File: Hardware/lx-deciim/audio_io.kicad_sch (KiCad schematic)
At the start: 35 parts, among them J13 AudioJack2_SwitchT, J14 AudioJack2_SwitchT, J15 AudioJack2_SwitchT, J16 AudioJack2_SwitchT, U5 TL074, U6 MCP6004

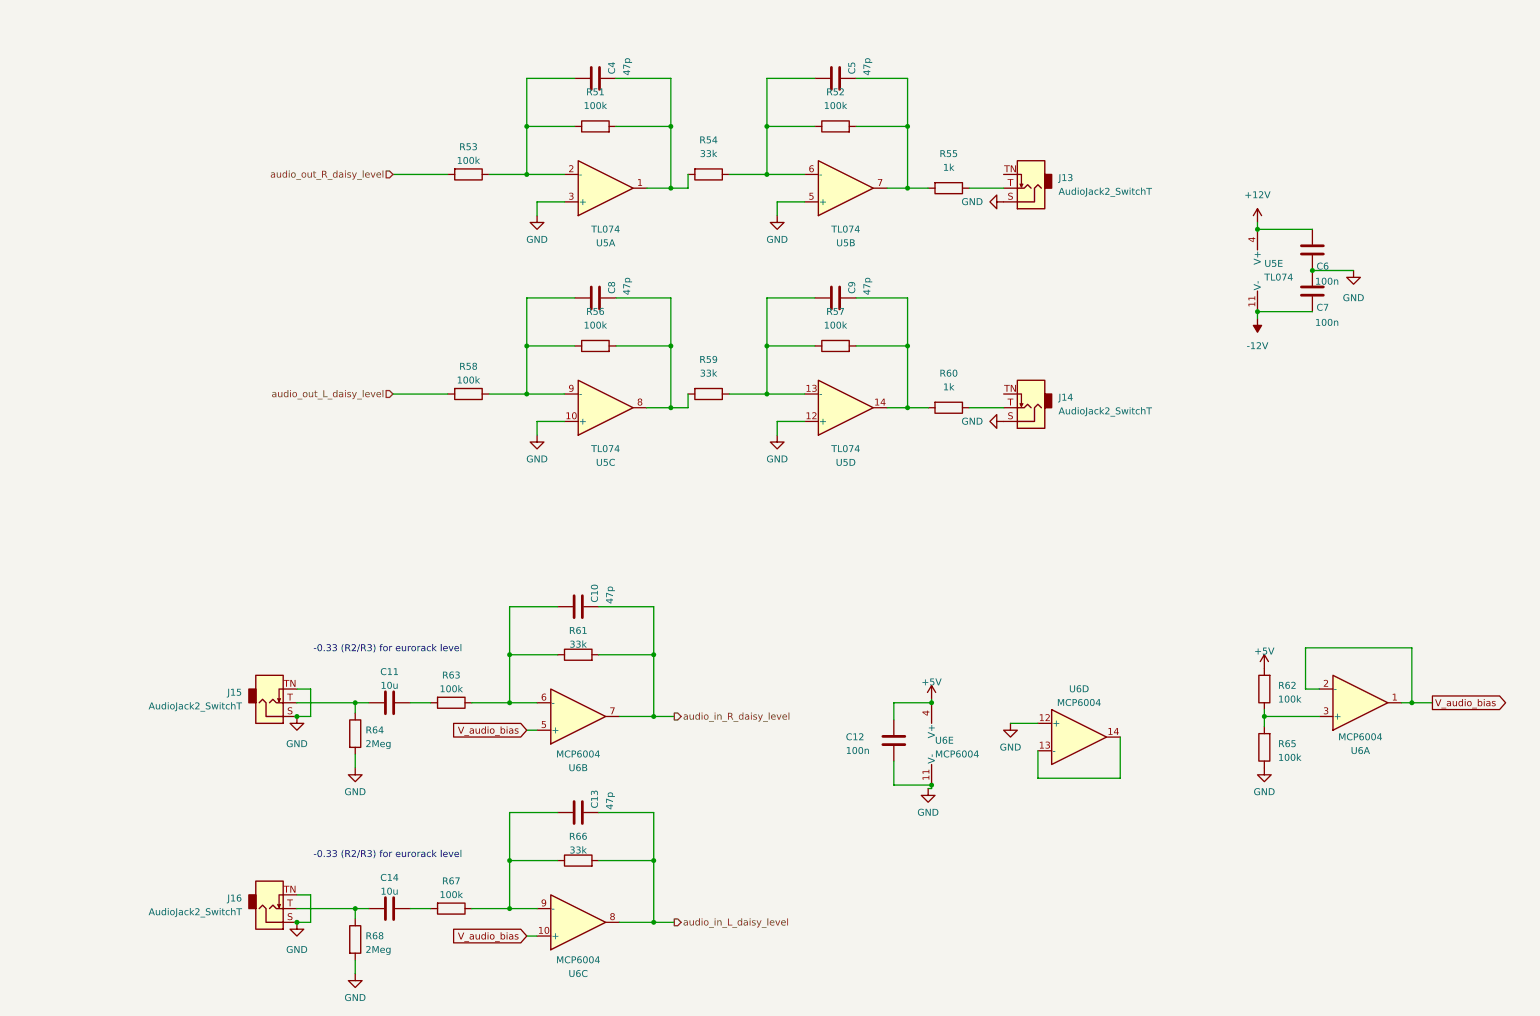
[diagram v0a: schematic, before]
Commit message: feature: first draft routing
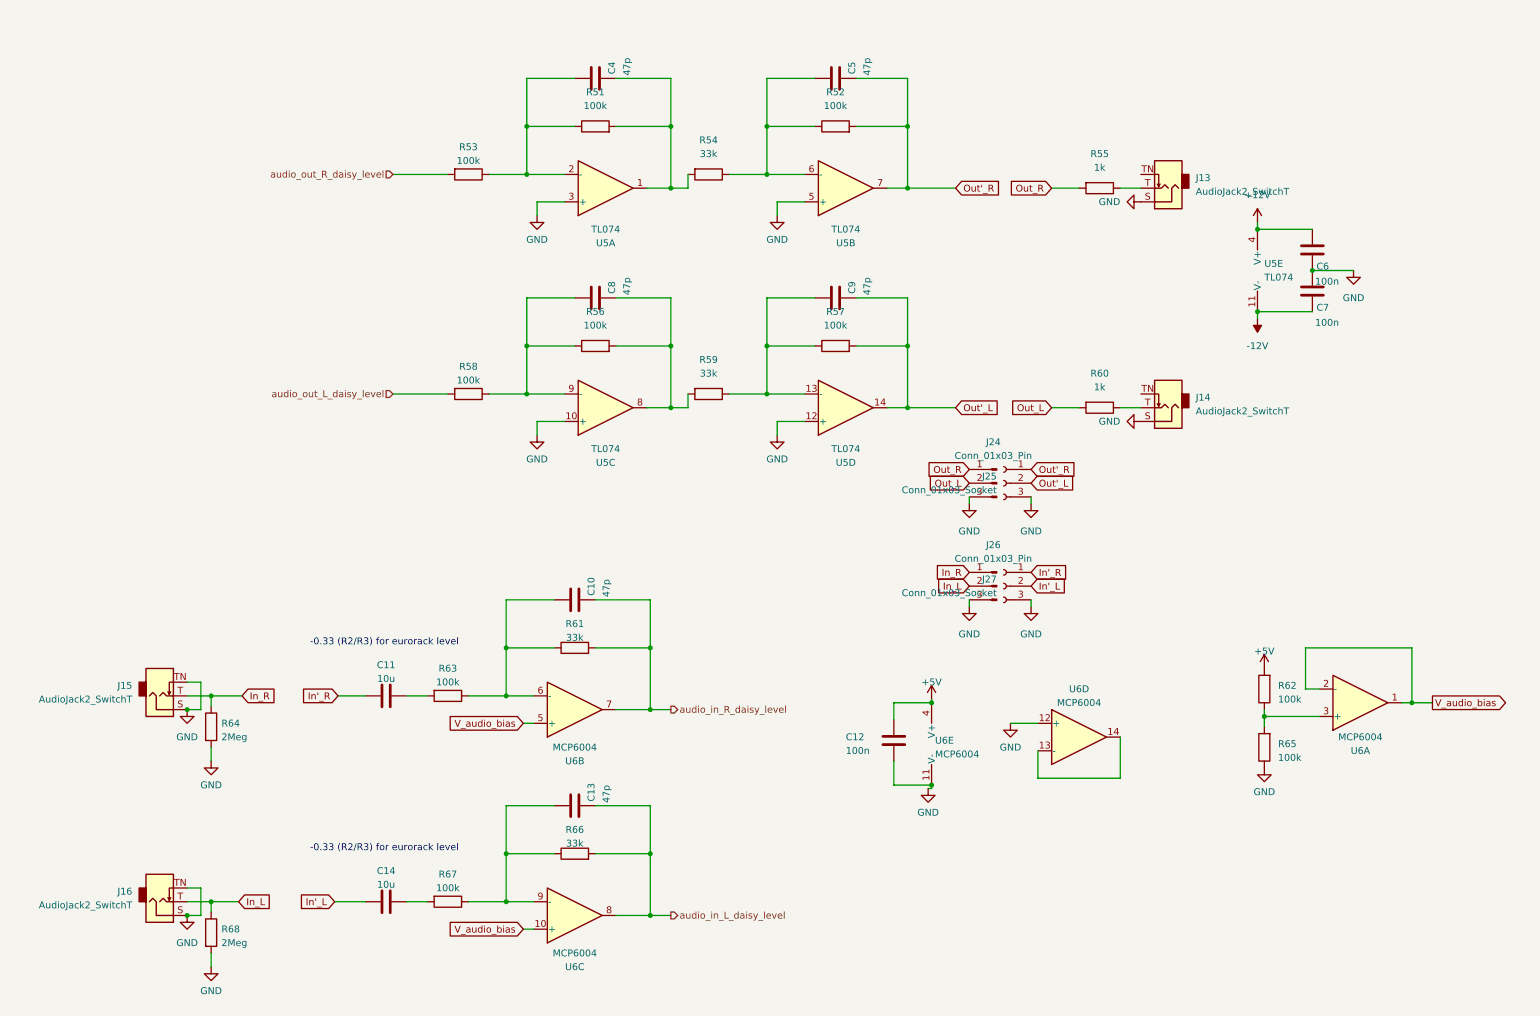
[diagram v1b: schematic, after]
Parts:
- added J24, J26: Conn_01x03_Pin, Connector_PinHeader_2.54mm:PinHeader_1x03_P2.54mm_Vertical, symbol Connector:Conn_01x03_Pin
- added J25, J27: Conn_01x03_Socket, Connector_PinSocket_2.54mm:PinSocket_1x03_P2.54mm_Vertical, symbol Connector:Conn_01x03_Socket
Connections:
- net GND: now also J24.3 (Pin_3), J25.3 (Pin_3), J26.3 (Pin_3), J27.3 (Pin_3)
- net Out'_R: now reaches C5.2, R52.2, U5.7
- net Out'_R: now also J25.1 (Pin_1); no longer R55.2
- net Out'_L: now reaches C9.2, R57.2, U5.14
- net Out'_L: now also J25.2 (Pin_2); no longer R60.2
- net In_L: now reaches J16.T, R68.1
- net In_L: now also J26.2 (Pin_2); no longer C14.1
- net In_R: now reaches J15.T, R64.1
- net In_R: now also J26.1 (Pin_1); no longer C11.1
- new net In'_L: C14.1, J27.2 (Pin_2)
- new net In'_R: C11.1, J27.1 (Pin_1)
- new net Out_L: J24.2 (Pin_2), R60.2
- new net Out_R: J24.1 (Pin_1), R55.2
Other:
- moved on the sheet: C10, C11, C13, C14, J13, J14, J15, J16, R55, R60, R61, R63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

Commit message: feature: prep files for export (fill bom, gerber)
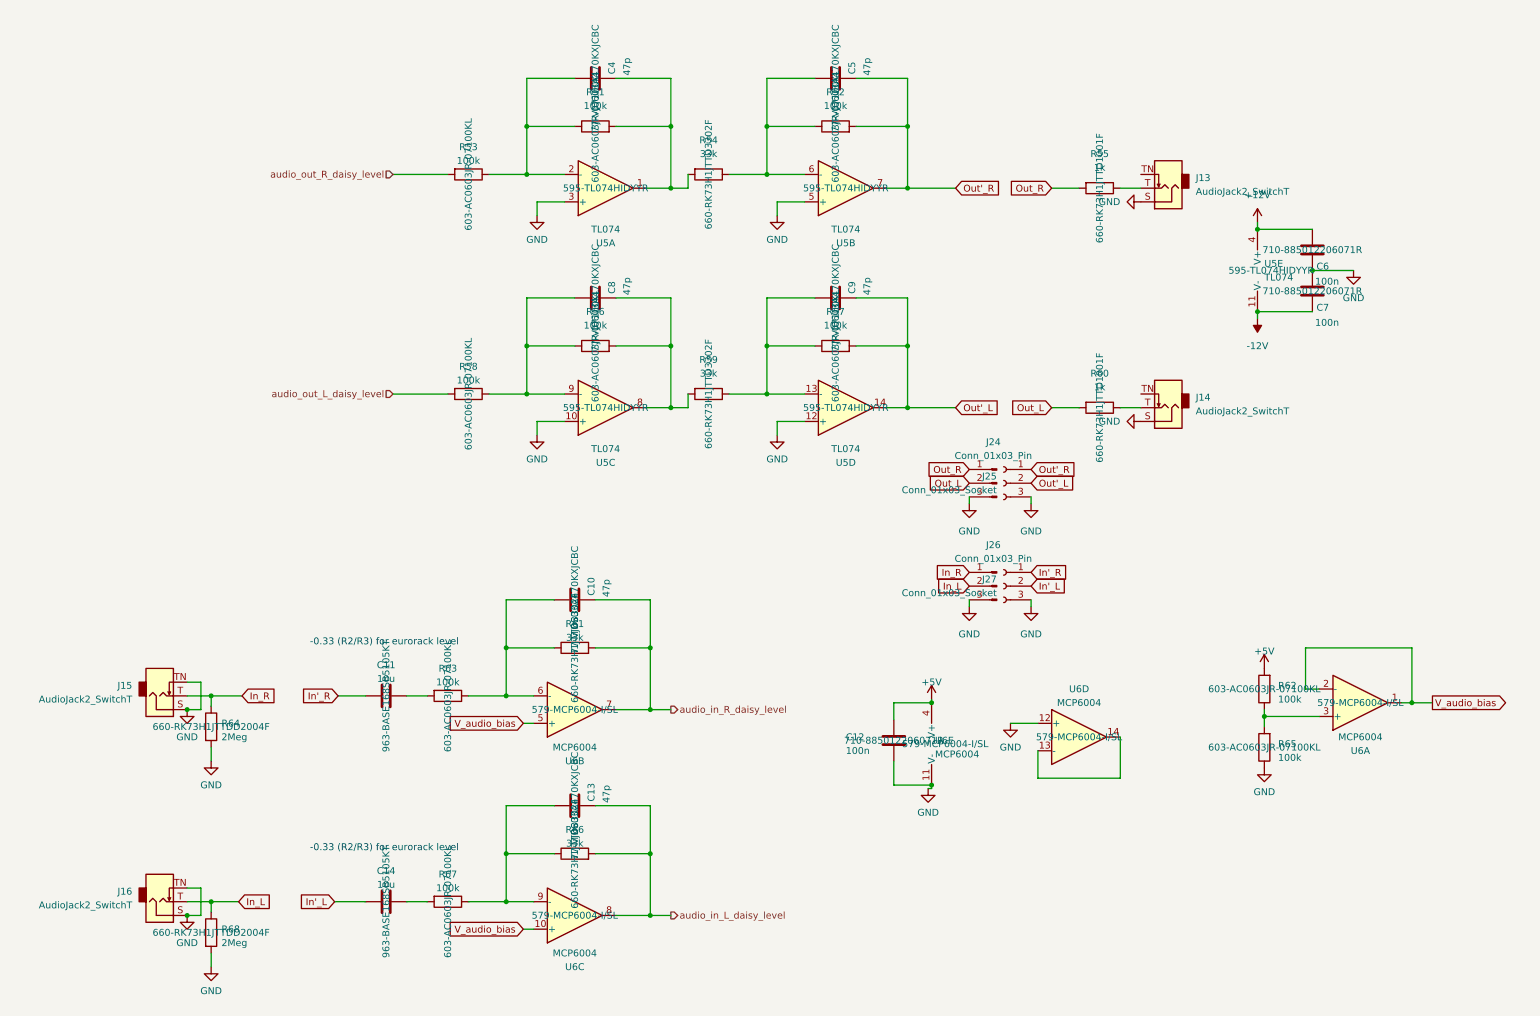
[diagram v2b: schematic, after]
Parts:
- C10, C13, C4, C5, C8, C9: Mouser Part Number (none) -> 77-VJ0603A470KXJCBC
- C11, C14: Mouser Part Number (none) -> 963-BASE168SB5105KT
- C12, C6, C7: Mouser Part Number (none) -> 710-885012206071R
- R51, R52, R53, R56, R57, R58, R62, R63, R65, R67: Mouser Part Number (none) -> 603-AC0603JR-07100KL
- R54, R59, R61, R66: Mouser Part Number (none) -> 660-RK73H1JTTD3302F
- R55, R60: Mouser Part Number (none) -> 660-RK73H1JTTD1001F
- R64, R68: Mouser Part Number (none) -> 660-RK73H1JTTDD2004F
- U5: Mouser Part Number (none) -> 595-TL074HIDYYR
- U6: Mouser Part Number (none) -> 579-MCP6004-I/SL

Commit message: fix: fix mouser part number on schematic + fill page settings
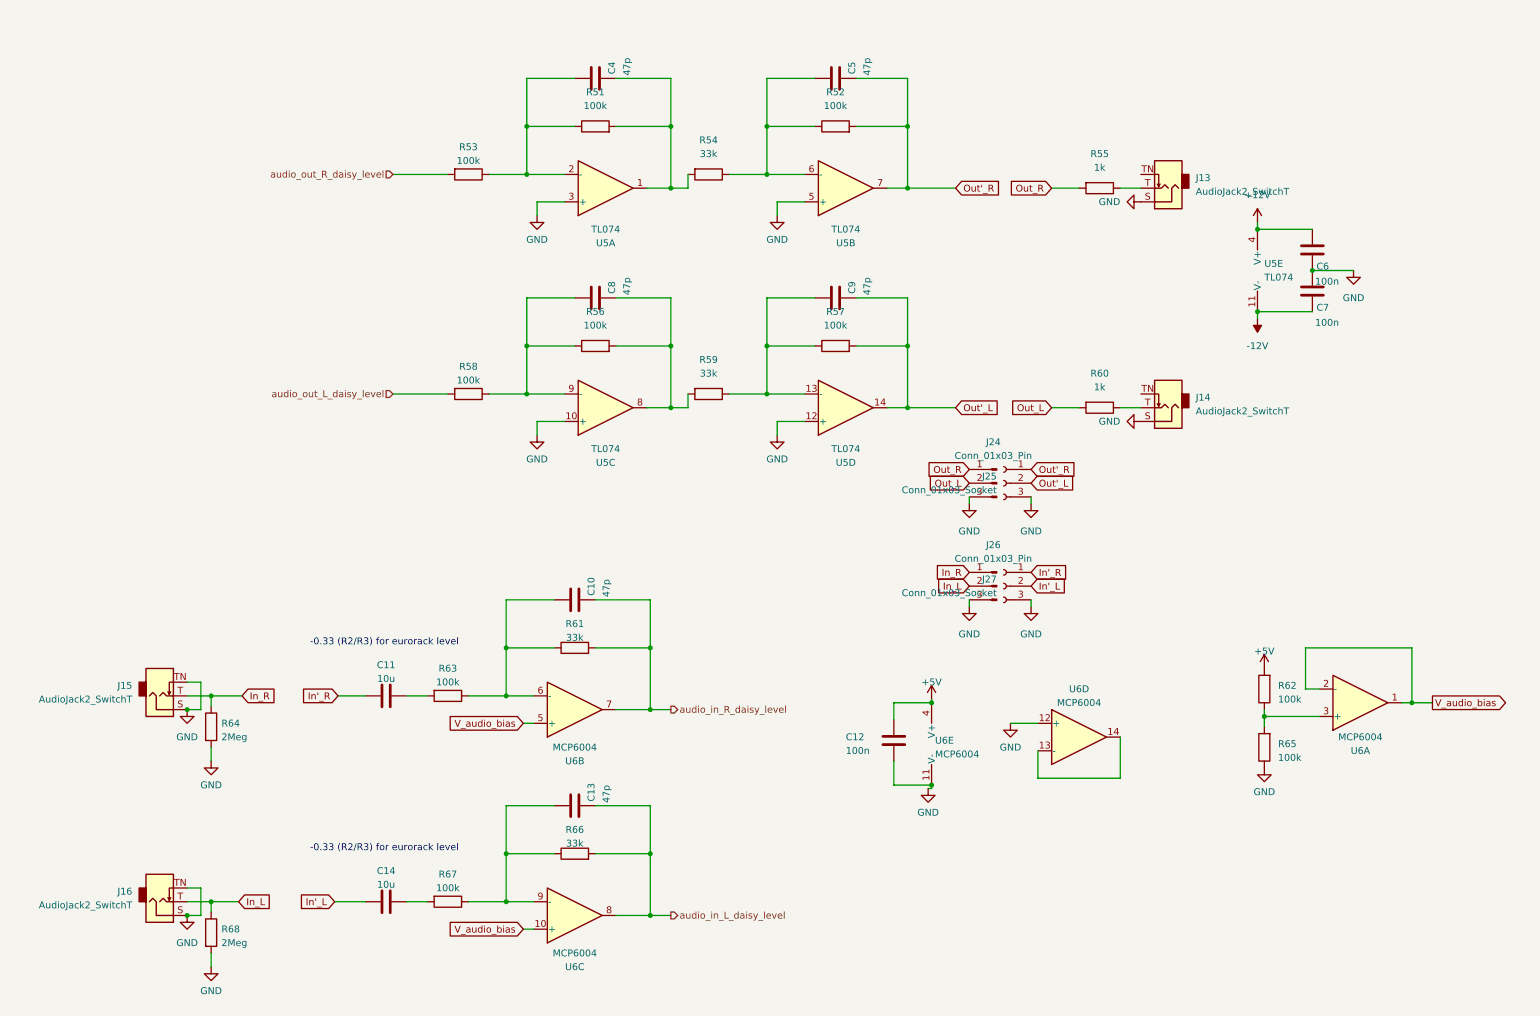
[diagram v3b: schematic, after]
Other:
- company: (none) -> Lucas Bonvin
- title: (none) -> lx-deciim
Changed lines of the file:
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@@
 	(generator_version "9.0")
 	(paper "A4")
+	(title_block
+		(title "lx-deciim")
+		(date "2025-06-17")
+		(rev "v1.0.0")
+		(company "Lucas Bonvin")
+		(comment 1 "This project is licensed under the CC BY-NC 4.0 License.")
+	)
 	(text "\n-0.33 (R2/R3) for eurorack level\n"
 		(exclude_from_sim no)
@@
 					(size 1.27 1.27)
 				)
+				(hide yes)
 			)
 		)
@@
 					(size 1.27 1.27)
 				)
+				(hide yes)
 			)
 		)
@@
 					(size 1.27 1.27)
 				)
+				(hide yes)
 			)
 		)
@@
 					(size 1.27 1.27)
 				)
+				(hide yes)
 			)
 		)
@@
 					(size 1.27 1.27)
 				)
+				(hide yes)
 			)
 		)
@@
 					(size 1.27 1.27)
 				)
+				(hide yes)
 			)
 		)
@@
 					(size 1.27 1.27)
 				)
+				(hide yes)
 			)
 		)
@@
 					(size 1.27 1.27)
 				)
+				(hide yes)
 			)
 		)
@@
 					(size 1.27 1.27)
 				)
+				(hide yes)
 			)
 		)
@@
 					(size 1.27 1.27)
 				)
+				(hide yes)
 			)
 		)
@@
 					(size 1.27 1.27)
 				)
+				(hide yes)
 			)
 		)
@@
 					(size 1.27 1.27)
 				)
+				(hide yes)
 			)
 		)
@@
 					(size 1.27 1.27)
 				)
+				(hide yes)
 			)
 		)
@@
 					(size 1.27 1.27)
 				)
+				(hide yes)
 			)
 		)
@@
 					(size 1.27 1.27)
 				)
+				(hide yes)
 			)
 		)
@@
 					(size 1.27 1.27)
 				)
+				(hide yes)
 			)
 		)
@@
 					(size 1.27 1.27)
 				)
+				(hide yes)
 			)
 		)
@@
 					(size 1.27 1.27)
 				)
+				(hide yes)
 			)
 		)
@@
 					(size 1.27 1.27)
 				)
+				(hide yes)
 			)
 		)
@@
 					(size 1.27 1.27)
 				)
+				(hide yes)
 			)
 		)
@@
 					(size 1.27 1.27)
 				)
+				(hide yes)
 			)
 		)
@@
 					(size 1.27 1.27)
 				)
+				(hide yes)
 			)
 		)
@@
 					(size 1.27 1.27)
 				)
+				(hide yes)
 			)
 		)
@@
 					(size 1.27 1.27)
 				)
+				(hide yes)
 			)
 		)
@@
 					(size 1.27 1.27)
 				)
+				(hide yes)
 			)
 		)
@@
 					(size 1.27 1.27)
 				)
+				(hide yes)
 			)
 		)
@@
 					(size 1.27 1.27)
 				)
+				(hide yes)
 			)
 		)
@@
 					(size 1.27 1.27)
 				)
+				(hide yes)
 			)
 		)
@@
 					(size 1.27 1.27)
 				)
+				(hide yes)
 			)
 		)
@@
 					(size 1.27 1.27)
 				)
+				(hide yes)
 			)
 		)
@@
 					(size 1.27 1.27)
 				)
+				(hide yes)
 			)
 		)
@@
 					(size 1.27 1.27)
 				)
+				(hide yes)
 			)
 		)
@@
 					(size 1.27 1.27)
 				)
+				(hide yes)
 			)
 		)
@@
 					(size 1.27 1.27)
 				)
+				(hide yes)
 			)
 		)
@@
 					(size 1.27 1.27)
 				)
+				(hide yes)
 			)
 		)
@@
 					(size 1.27 1.27)
 				)
+				(hide yes)
 			)
 		)
@@
 					(size 1.27 1.27)
 				)
+				(hide yes)
 			)
 		)
@@
 					(size 1.27 1.27)
 				)
+				(hide yes)
 			)
 		)
@@
 					(size 1.27 1.27)
 				)
+				(hide yes)
 			)
 		)
